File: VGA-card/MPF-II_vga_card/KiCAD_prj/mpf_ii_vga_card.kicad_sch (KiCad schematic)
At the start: 1 part, among them J1 Bus_Apple_II_Card_Side

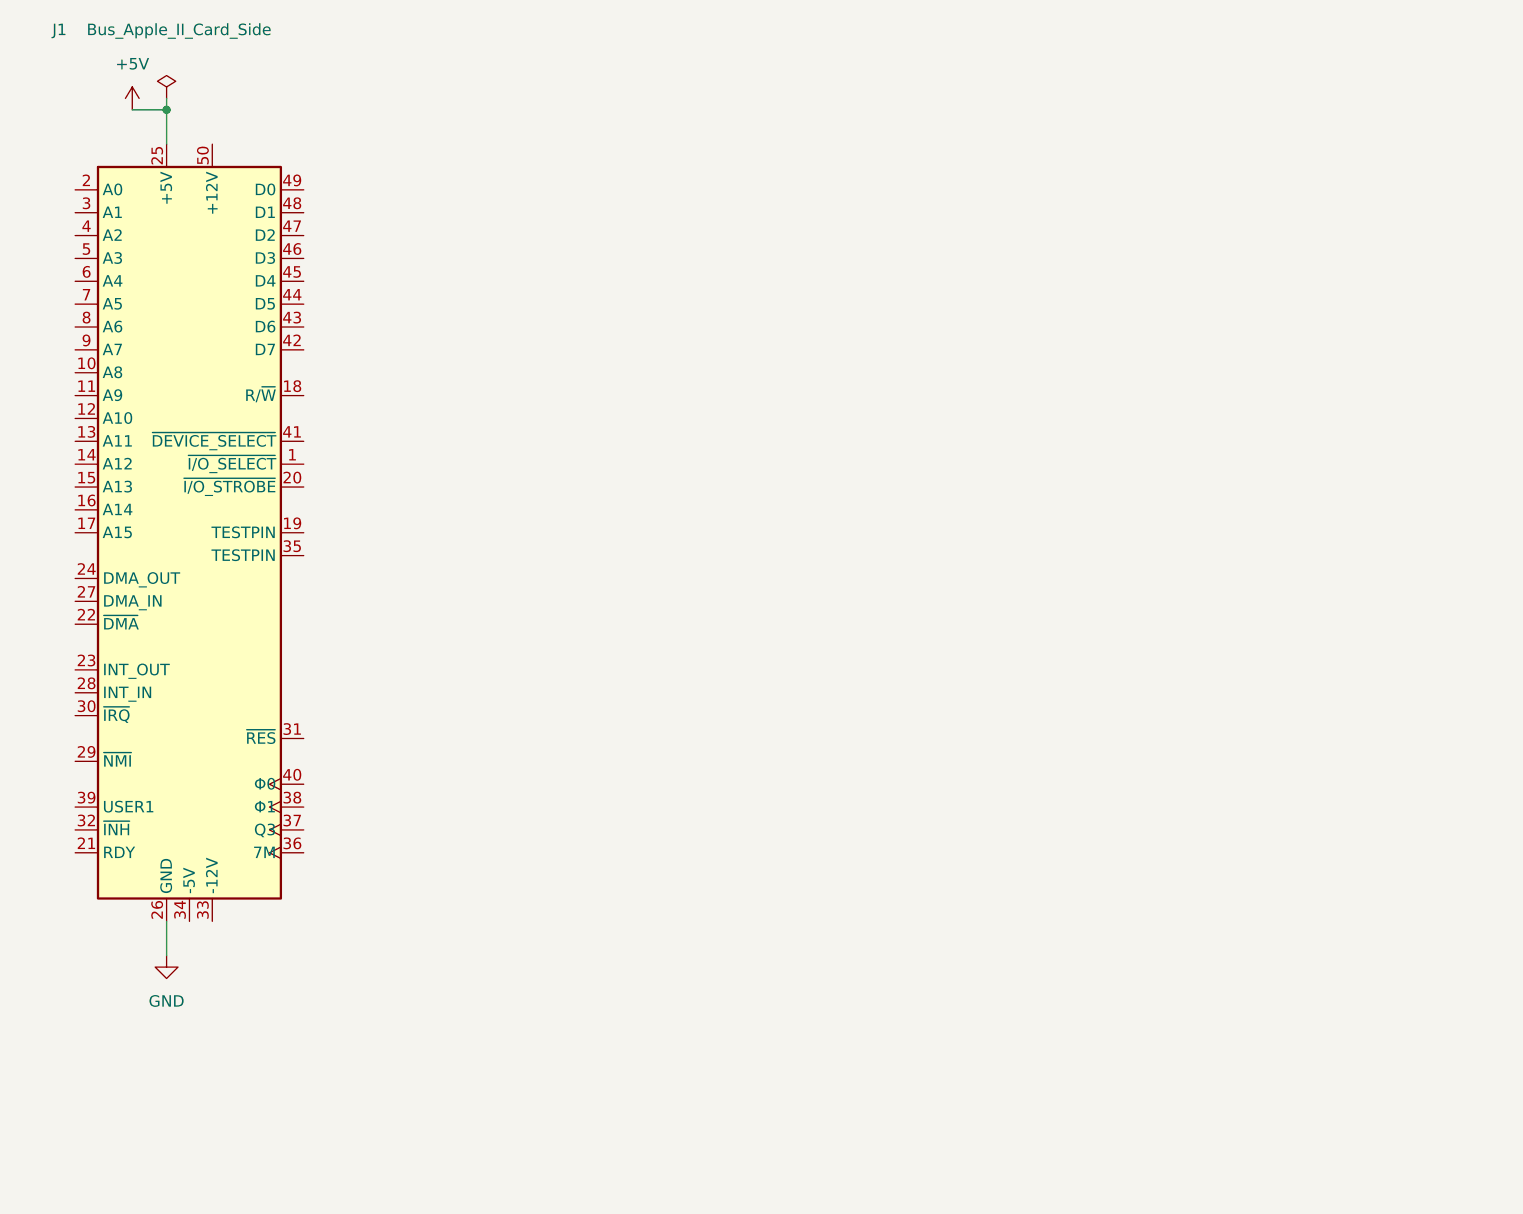
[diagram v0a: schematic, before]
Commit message: VGA card schematics updated
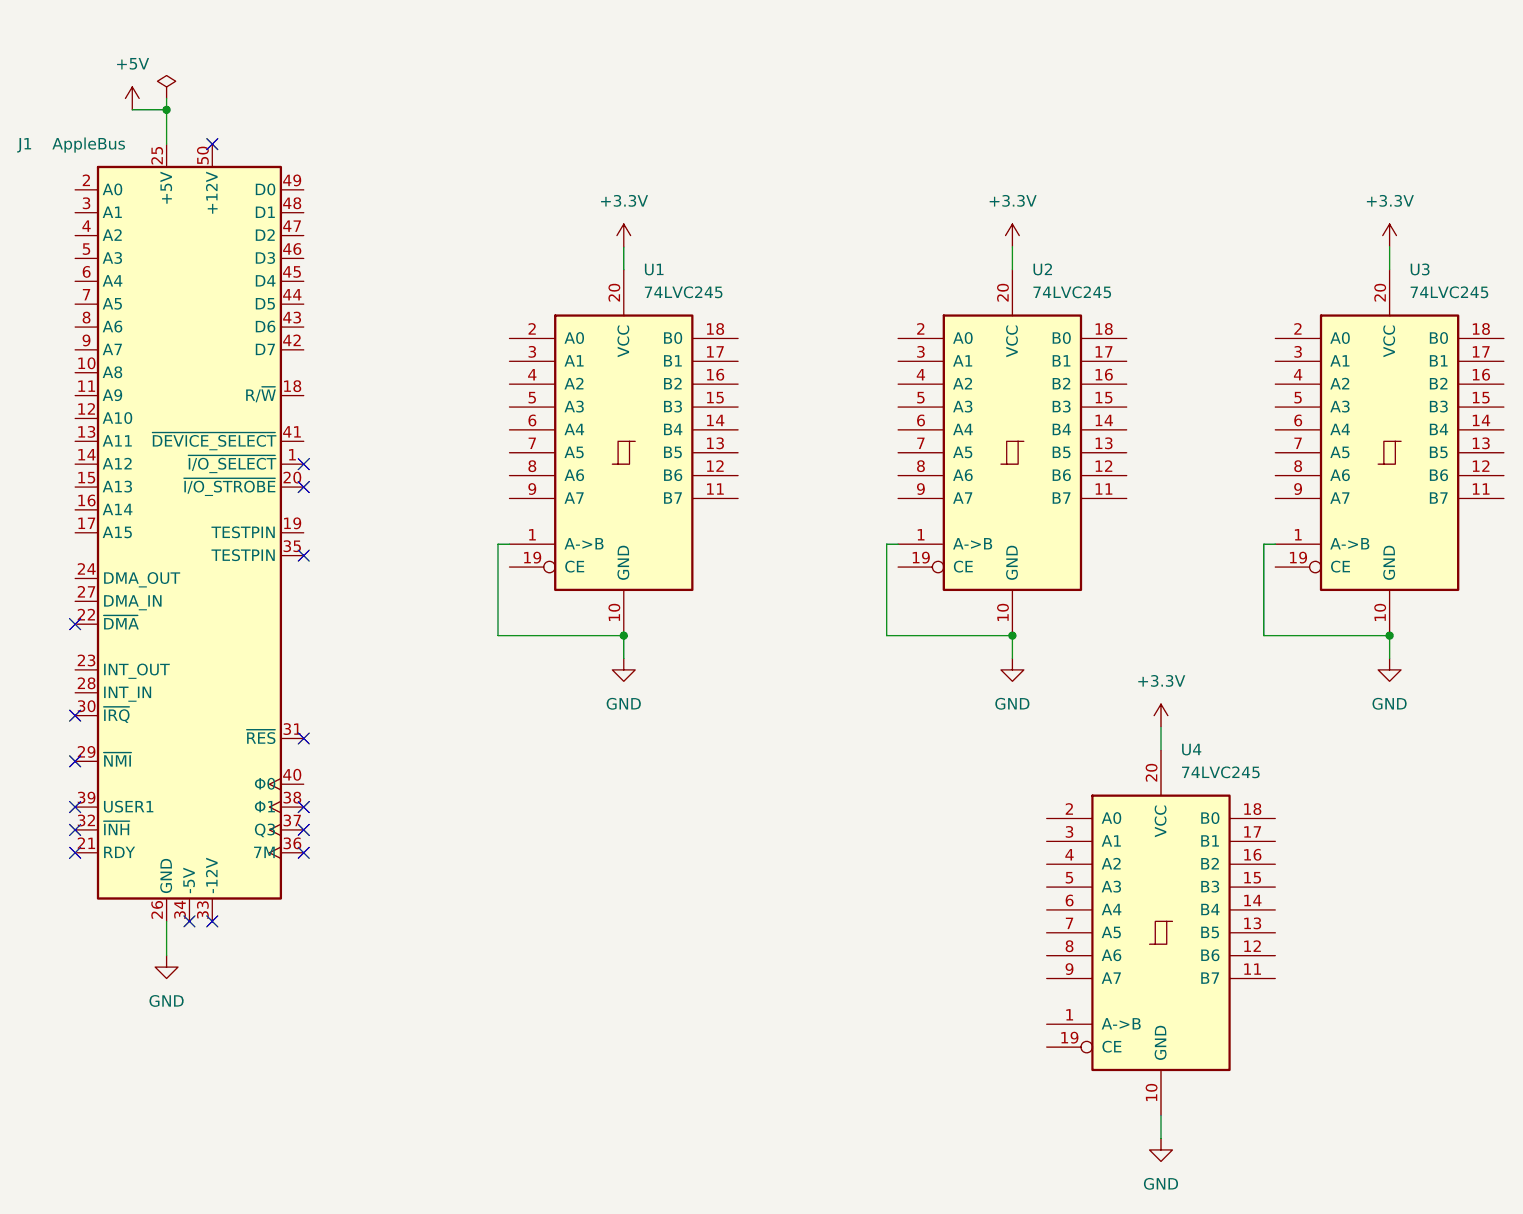
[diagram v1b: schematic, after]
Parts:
- added U1, U2, U3, U4: 74LVC245, Package_DIP:DIP-20_W7.62mm, symbol 74xx:74LS245
- J1: value Bus_Apple_II_Card_Side -> AppleBus
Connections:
- net GND: now also U1.1 (A->B), U1.10 (GND), U2.1 (A->B), U2.10 (GND), U3.1 (A->B), U3.10 (GND), U4.10 (GND)
- new net +3.3V: U1.20 (VCC), U2.20 (VCC), U3.20 (VCC), U4.20 (VCC)
- no-connect marks 0 -> 16
